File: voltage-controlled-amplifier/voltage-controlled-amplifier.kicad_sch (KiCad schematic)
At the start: 27 parts, among them J1 Power, J10 Output 2, J2 Power, J3 Pot, J4 Input 1, J5 CV 1, J6 Output 1, J7 Pot, J8 Input 2, J9 CV 2, U1 LM13700

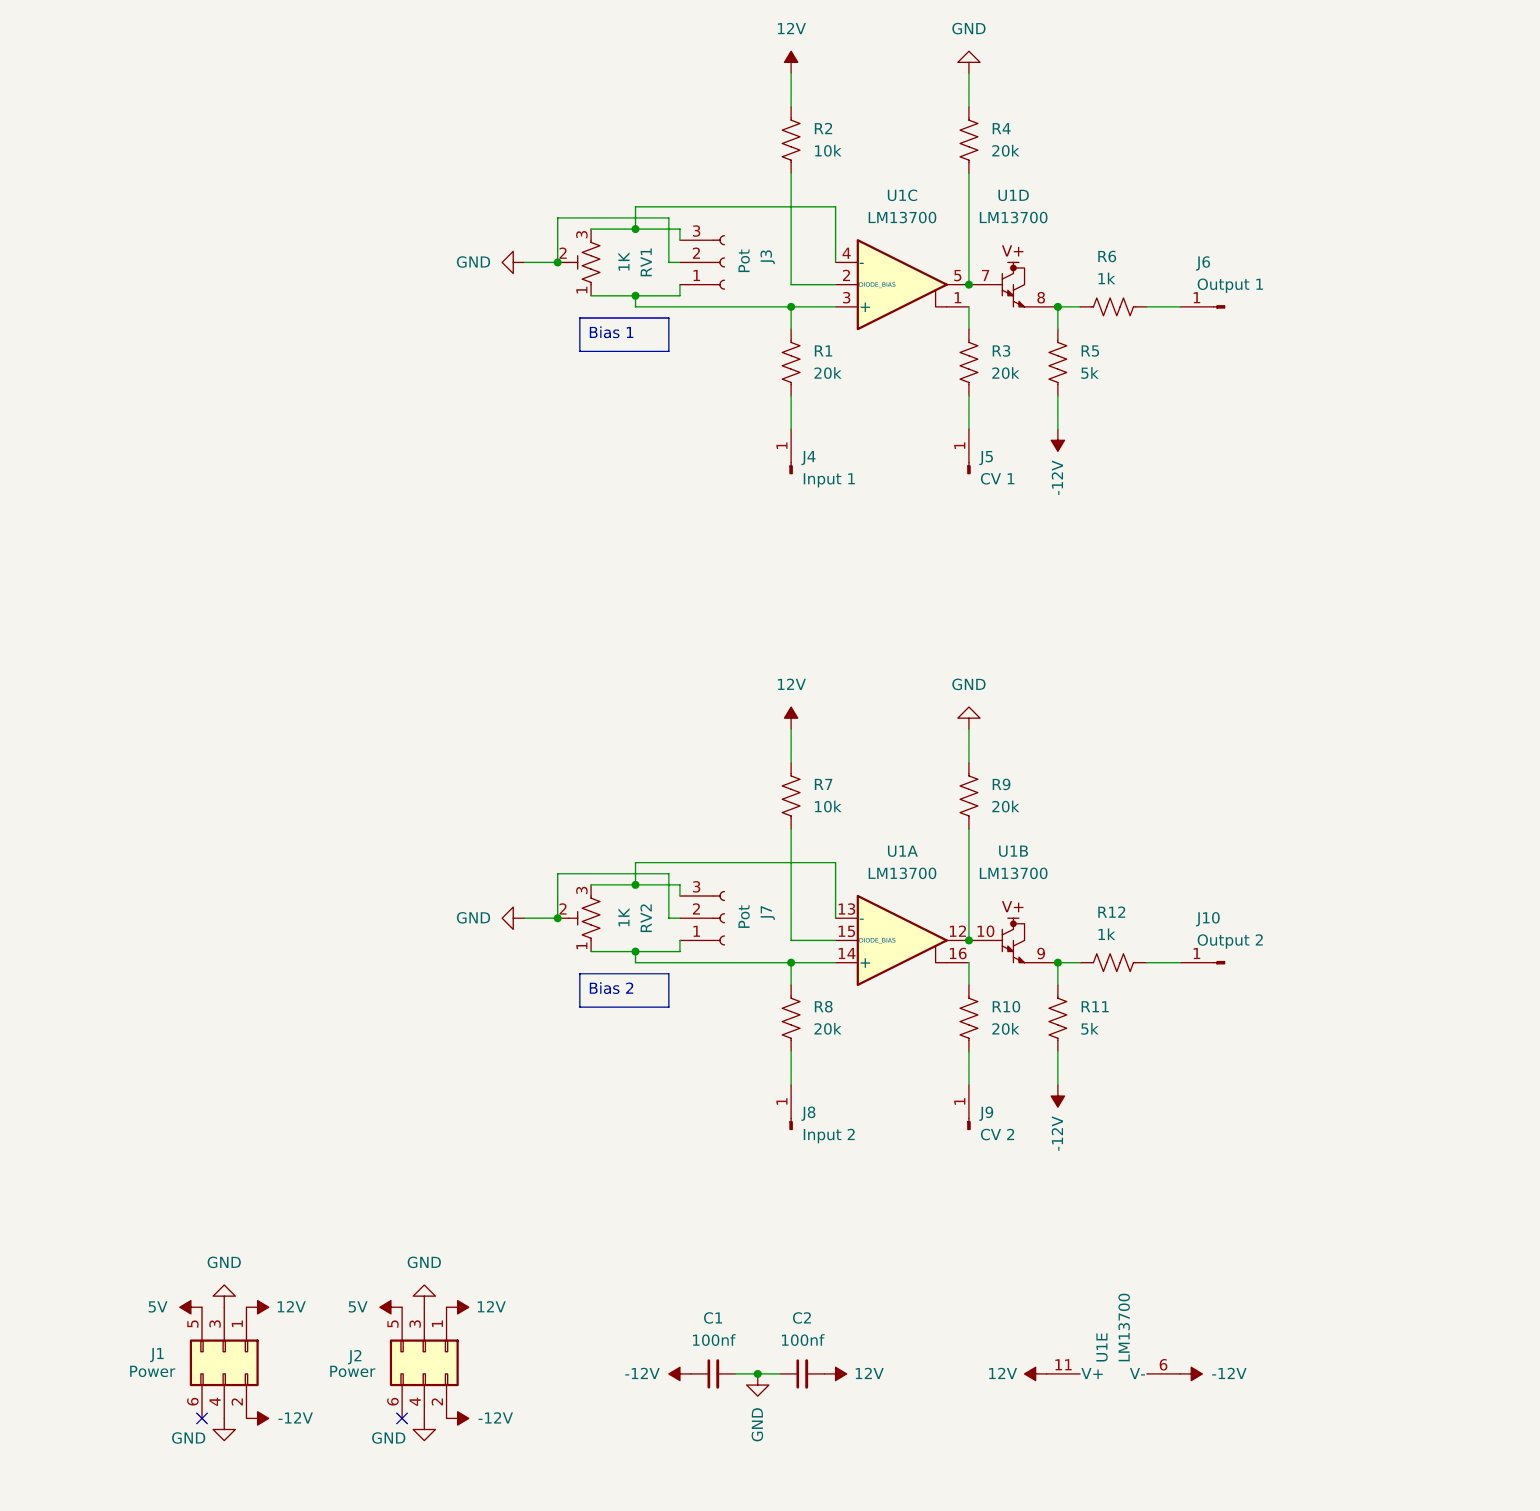
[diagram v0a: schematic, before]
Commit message: Buffer output of vca
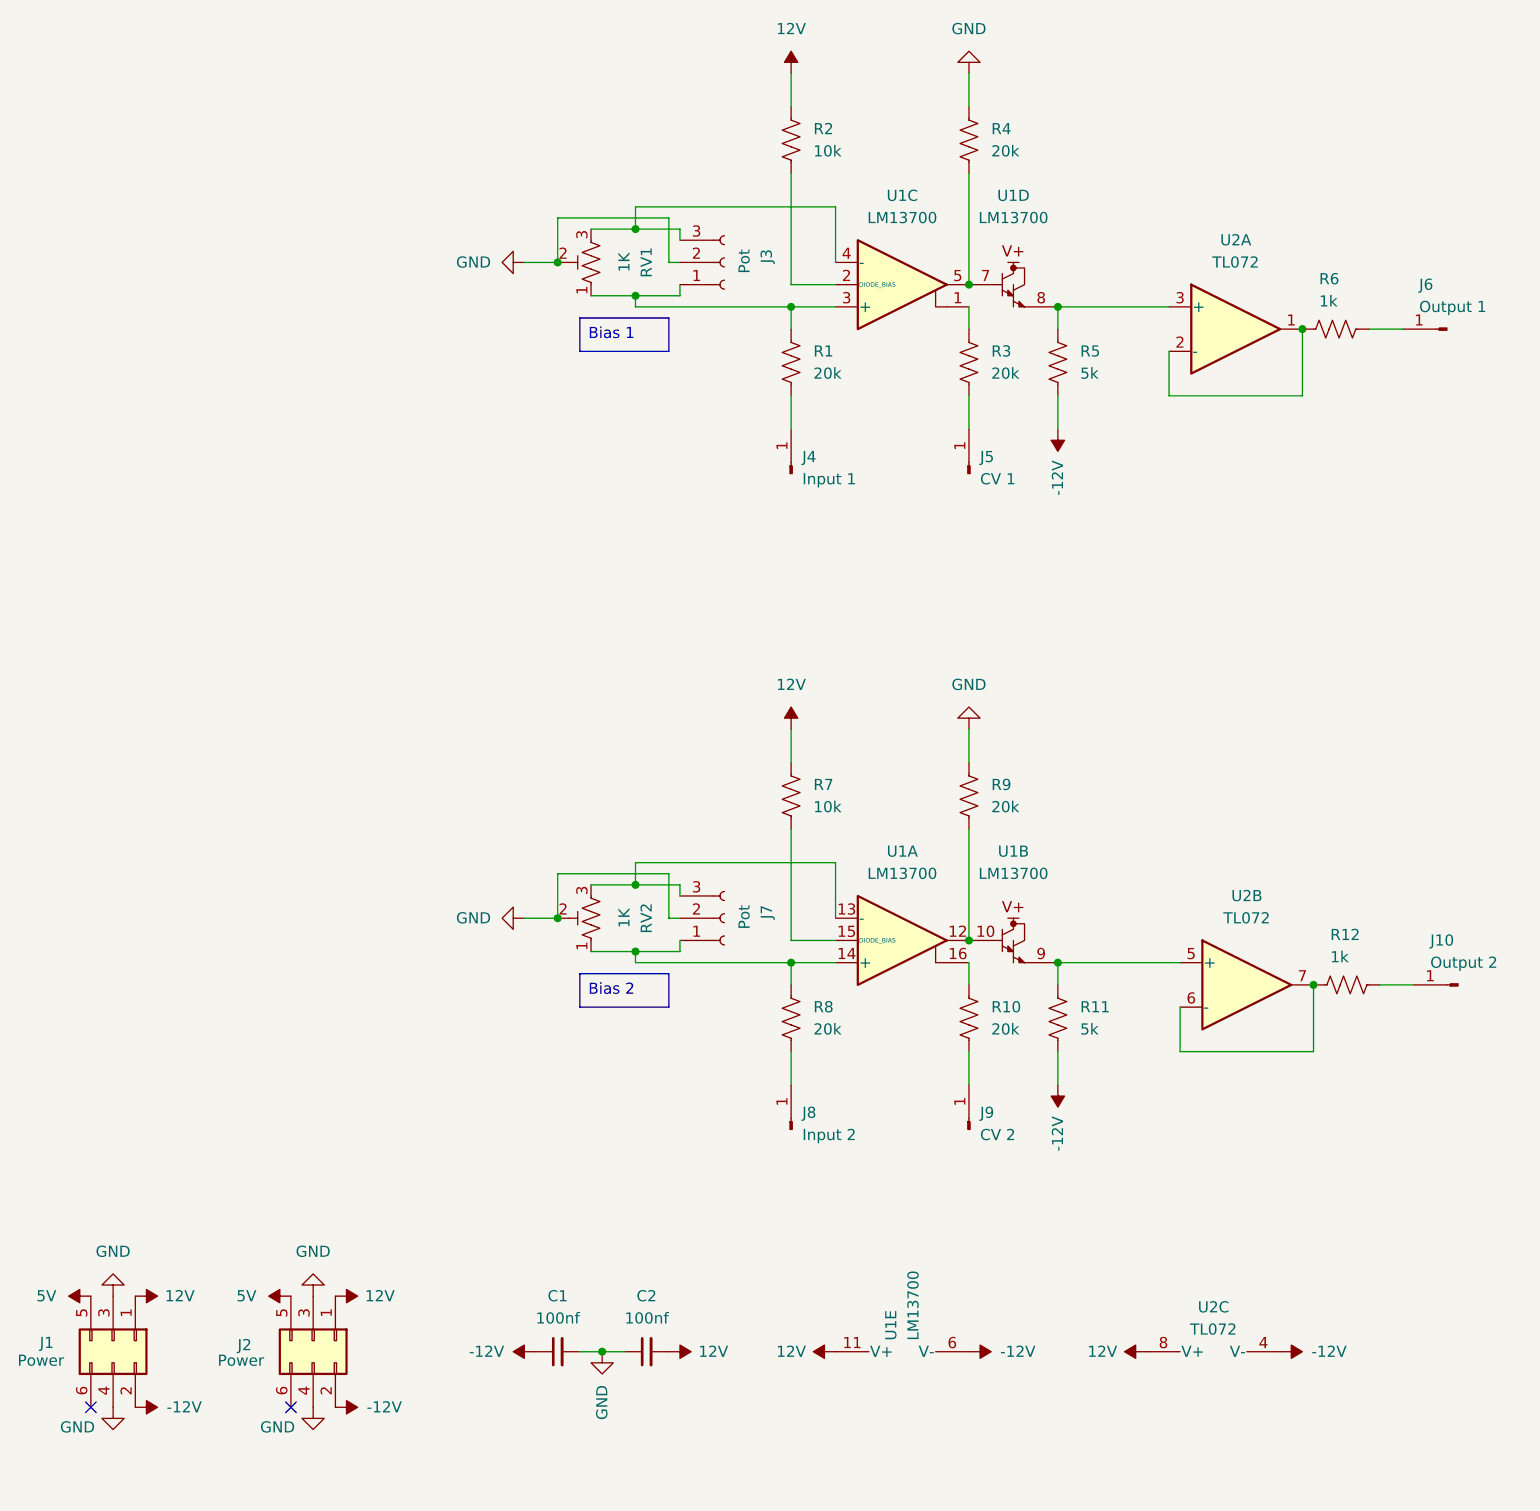
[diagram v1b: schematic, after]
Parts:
- added U2: TL072, Package_DIP:DIP-8_W7.62mm_Socket, symbol Amplifier_Operational:TL072
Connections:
- net -12V: now also U2.4 (V-)
- net 12V: now also U2.8 (V+)
- net at R11.1, U1.9: now also U2.5 (+); no longer R12.1
- net at R5.1, U1.8: now also U2.3 (+); no longer R6.1
- new net: R12.1, U2.6 (-), U2.7
- new net: R6.1, U2.1, U2.2 (-)
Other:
- moved on the sheet: C1, C2, J1, J10, J2, J6, R12, R6, U1E

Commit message: Various improvements
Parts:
- added C3, C4: 100nf, Capacitor_THT:C_Disc_D4.3mm_W1.9mm_P5.00mm, symbol Device:C_Small
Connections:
- net -12V: now also C2.1, C4.1; no longer C1.1
- net 12V: now also C1.2, C3.2; no longer C2.2
- net GND: now also C1.1, C2.2, C3.1, C4.2; no longer C1.2, C2.1

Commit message: Vca fixes
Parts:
- R11, R5: value 5k -> 5.1k
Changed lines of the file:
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@@
 			)
 		)
-		(property "Value" "5k"
+		(property "Value" "5.1k"
 			(at 142.24 62.2299 0)
 			(effects
@@
 			)
 		)
-		(property "Value" "5k"
+		(property "Value" "5.1k"
 			(at 142.24 137.1599 0)
 			(effects
